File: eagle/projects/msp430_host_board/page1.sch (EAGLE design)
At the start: 5 parts, among them U1 Value

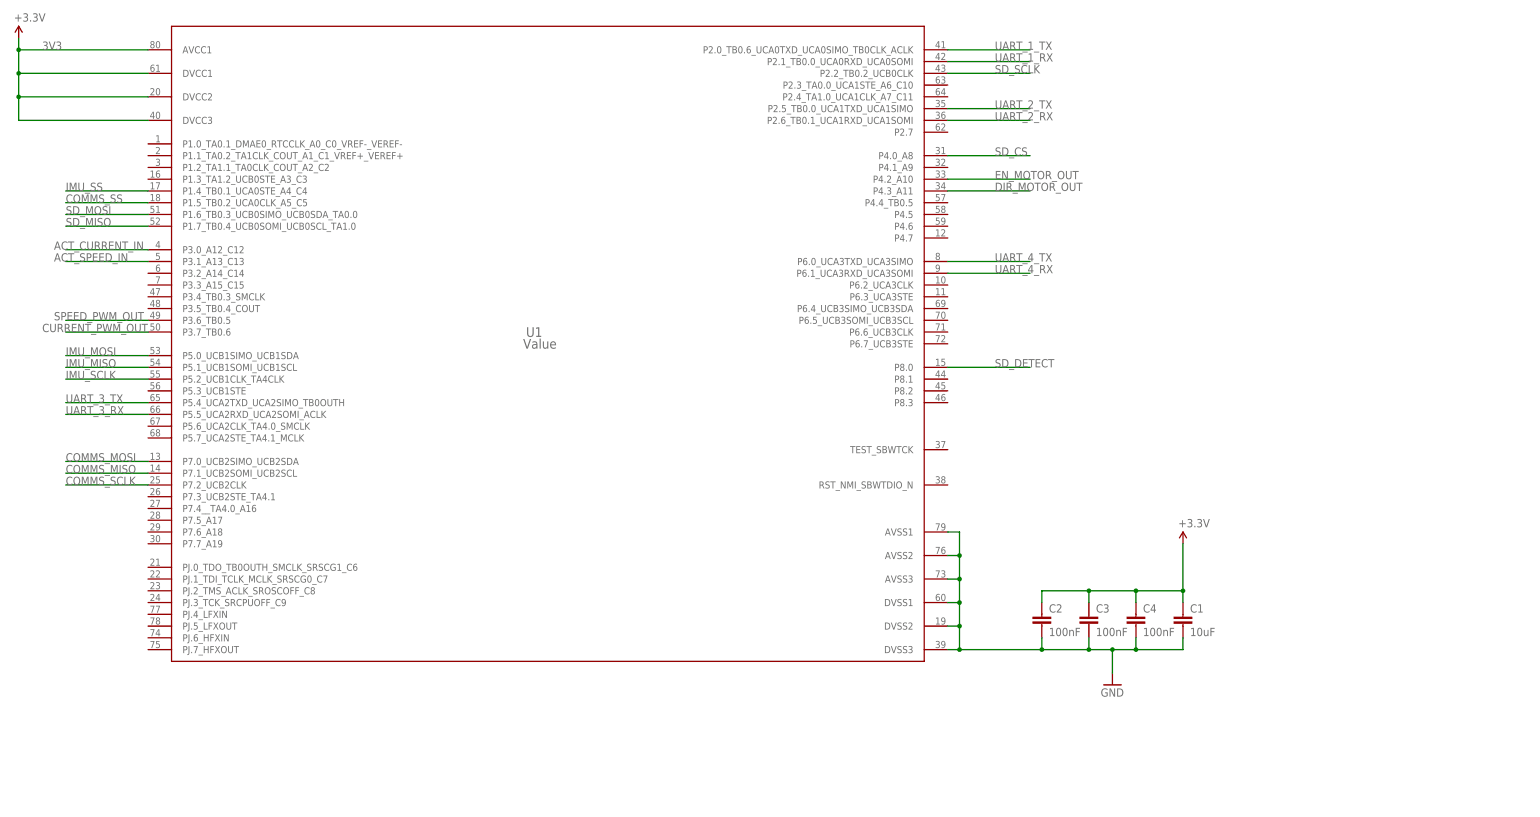
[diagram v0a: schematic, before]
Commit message: Added 22pf cap and LF crystal to schematic
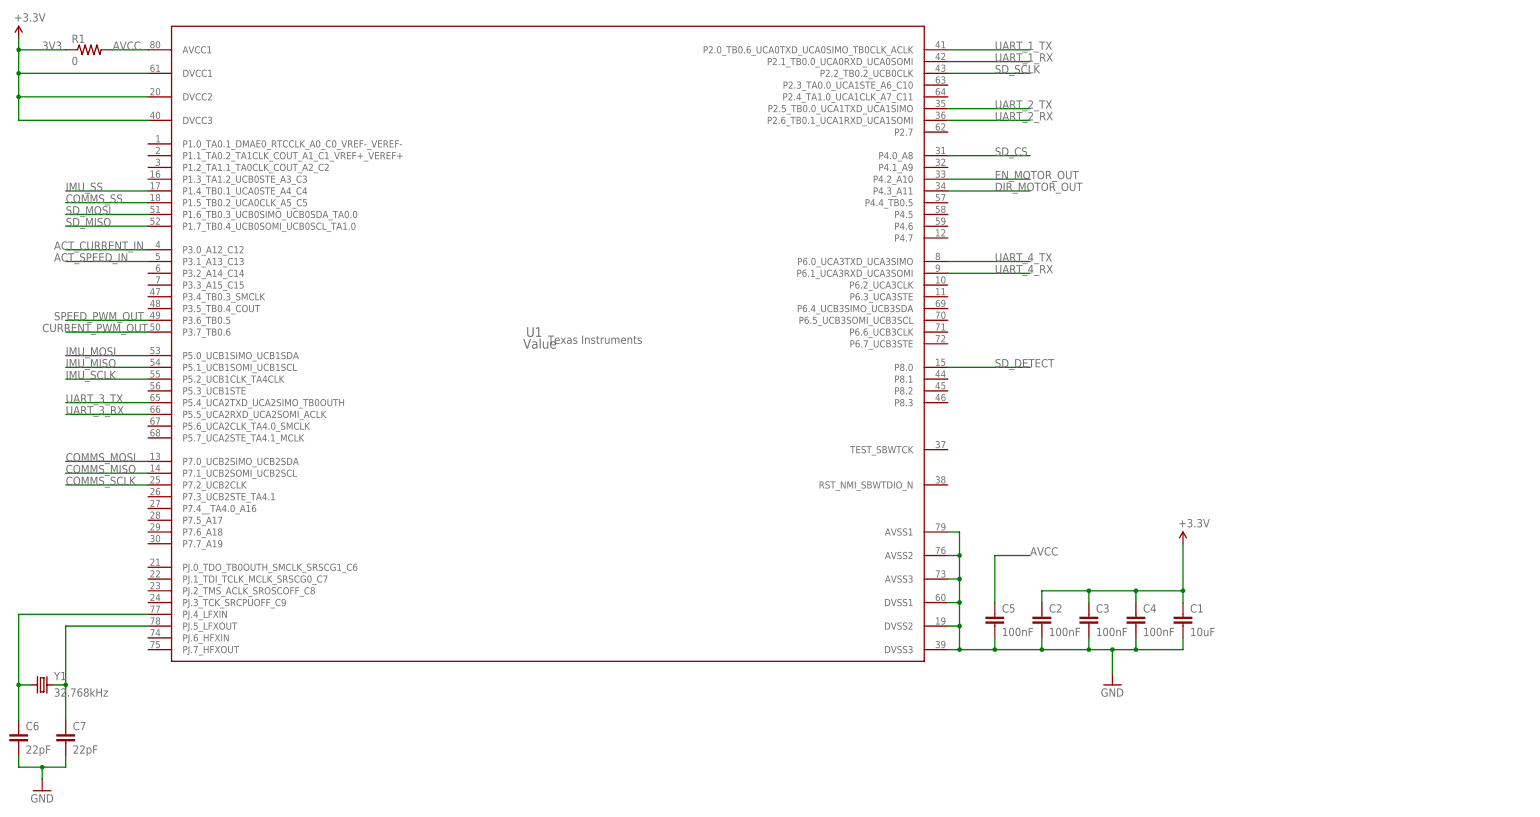
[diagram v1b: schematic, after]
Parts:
- added C5: 100nF, daqcs_host:CAP_100NF0_0603
- added C6, C7: 22pF, daqcs_host:CAP_22PF0_0603
- added R1: 0, daqcs_host:RES_0R0_0603
- added Y1: 32.768kHz, SparkFun-FreqCtrl:CRYSTAL3.2X1.5MM
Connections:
- new net AVCC: C5.1, R1.2, U1.AVCC1
- new net N$1: C6.1, U1.PJ.4_LFXIN, Y1.1
- new net N$2: C7.1, U1.PJ.5_LFXOUT, Y1.2
- net 3V3: now also R1.1; no longer U1.AVCC1
- net GND: now also C5.2, C6.2, C7.2
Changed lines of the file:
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@@
 <setting verticaltext="up"/>
 </settings>
-<grid distance="0.1" unitdist="inch" unit="inch" style="dots" multiple="1" display="yes" altdistance="0.01" altunitdist="inch" altunit="inch"/>
+<grid distance="0.1" unitdist="inch" unit="inch" style="lines" multiple="1" display="no" altdistance="0.01" altunitdist="inch" altunit="inch"/>
 <layers>
 <layer number="1" name="Top" color="4" fill="1" visible="no" active="no"/>
@@
 <part name="C4" library="daqcs_host" deviceset="CAP" device="_0603" technology="_100NF0" value="100nF"/>
 <part name="GND1" library="SparkFun-Aesthetics" deviceset="GND" device=""/>
+<part name="R1" library="daqcs_host" deviceset="RES" device="_0603" technology="_0R0" value="0"/>
+<part name="C5" library="daqcs_host" deviceset="CAP" device="_0603" technology="_100NF0" value="100nF"/>
+<part name="Y1" library="SparkFun-FreqCtrl" deviceset="CRYSTAL" device="3.2X1.5MM" value="32.768kHz"/>
+<part name="C6" library="daqcs_host" deviceset="CAP" device="_0603" technology="_22PF0" value="22pF"/>
+<part name="C7" library="daqcs_host" deviceset="CAP" device="_0603" technology="_22PF0" value="22pF"/>
+<part name="GND2" library="SparkFun-Aesthetics" deviceset="GND" device=""/>
 </parts>
 <sheets>
@@
 </plain>
 <instances>
-<instance part="U1" gate="A" x="43.18" y="48.26"/>
+<instance part="U1" gate="A" x="43.18" y="48.26">
+<attribute name="MANUFACTURER" x="43.18" y="48.26" size="1.778" layer="96"/>
+<attribute name="PARTNUMBER" x="43.18" y="48.26" size="1.778" layer="96" display="off"/>
+</instance>
 <instance part="FRAME1" gate="G$1" x="-78.74" y="-55.88"/>
 <instance part="3V3" gate="G$1" x="-71.12" y="114.3"/>
@@
 <instance part="C4" gate="G$1" x="170.18" y="-12.7"/>
 <instance part="GND1" gate="1" x="165.1" y="-25.4"/>
+<instance part="R1" gate="G$1" x="-55.88" y="111.76"/>
+<instance part="C5" gate="G$1" x="139.7" y="-12.7"/>
+<instance part="Y1" gate="G$1" x="-66.04" y="-25.4"/>
+<instance part="C6" gate="G$1" x="-71.12" y="-38.1"/>
+<instance part="C7" gate="G$1" x="-60.96" y="-38.1"/>
+<instance part="GND2" gate="1" x="-66.04" y="-48.26"/>
 </instances>
 <busses>
@@
 <pinref part="3V3" gate="G$1" pin="3.3V"/>
 <wire x1="-71.12" y1="114.3" x2="-71.12" y2="111.76" width="0.1524" layer="91"/>
-<pinref part="U1" gate="A" pin="AVCC1"/>
-<wire x1="-71.12" y1="111.76" x2="-43.18" y2="111.76" width="0.1524" layer="91"/>
+<pinref part="U1" gate="A" pin="DVCC1"/>
 <wire x1="-71.12" y1="111.76" x2="-71.12" y2="106.68" width="0.1524" layer="91"/>
-<junction x="-71.12" y="111.76"/>
-<pinref part="U1" gate="A" pin="DVCC1"/>
 <wire x1="-71.12" y1="106.68" x2="-43.18" y2="106.68" width="0.1524" layer="91"/>
 <wire x1="-71.12" y1="106.68" x2="-71.12" y2="101.6" width="0.1524" layer="91"/>
@@
 <wire x1="-71.12" y1="96.52" x2="-43.18" y2="96.52" width="0.1524" layer="91"/>
 <label x="-66.04" y="111.76" size="1.778" layer="95"/>
+<pinref part="R1" gate="G$1" pin="1"/>
+<wire x1="-60.96" y1="111.76" x2="-71.12" y2="111.76" width="0.1524" layer="91"/>
+<junction x="-71.12" y="111.76"/>
 </segment>
 <segment>
@@
 <pinref part="U1" gate="A" pin="DVSS3"/>
 <wire x1="129.54" y1="-17.78" x2="132.08" y2="-17.78" width="0.1524" layer="91"/>
-<wire x1="132.08" y1="-17.78" x2="149.86" y2="-17.78" width="0.1524" layer="91"/>
+<wire x1="132.08" y1="-17.78" x2="139.7" y2="-17.78" width="0.1524" layer="91"/>
+<wire x1="139.7" y1="-17.78" x2="149.86" y2="-17.78" width="0.1524" layer="91"/>
 <wire x1="149.86" y1="-17.78" x2="160.02" y2="-17.78" width="0.1524" layer="91"/>
 <wire x1="160.02" y1="-17.78" x2="165.1" y2="-17.78" width="0.1524" layer="91"/>
@@
 <wire x1="165.1" y1="-22.86" x2="165.1" y2="-17.78" width="0.1524" layer="91"/>
 <junction x="165.1" y="-17.78"/>
-</segment>
-</net>
+<pinref part="C5" gate="G$1" pin="2"/>
+<wire x1="139.7" y1="-15.24" x2="139.7" y2="-17.78" width="0.1524" layer="91"/>
+<junction x="139.7" y="-17.78"/>
+</segment>
+<segment>
+<pinref part="C6" gate="G$1" pin="2"/>
+<wire x1="-71.12" y1="-40.64" x2="-71.12" y2="-43.18" width="0.1524" layer="91"/>
+<wire x1="-71.12" y1="-43.18" x2="-66.04" y2="-43.18" width="0.1524" layer="91"/>
+<pinref part="C7" gate="G$1" pin="2"/>
+<wire x1="-66.04" y1="-43.18" x2="-60.96" y2="-43.18" width="0.1524" layer="91"/>
+<wire x1="-60.96" y1="-43.18" x2="-60.96" y2="-40.64" width="0.1524" layer="91"/>
+<pinref part="GND2" gate="1" pin="GND"/>
+<wire x1="-66.04" y1="-45.72" x2="-66.04" y2="-43.18" width="0.1524" layer="91"/>
+<junction x="-66.04" y="-43.18"/>
+</segment>
+</net>
+<net name="AVCC" class="0">
+<segment>
+<pinref part="R1" gate="G$1" pin="2"/>
+<pinref part="U1" gate="A" pin="AVCC1"/>
+<wire x1="-50.8" y1="111.76" x2="-43.18" y2="111.76" width="0.1524" layer="91"/>
+<label x="-50.8" y="111.76" size="1.778" layer="95"/>
+</segment>
+<segment>
+<pinref part="C5" gate="G$1" pin="1"/>
+<wire x1="139.7" y1="-7.62" x2="139.7" y2="2.54" width="0.1524" layer="91"/>
+<wire x1="139.7" y1="2.54" x2="147.32" y2="2.54" width="0.1524" layer="91"/>
+<label x="147.32" y="2.54" size="1.778" layer="95"/>
+</segment>
+</net>
+<net name="N$1" class="0">
+<segment>
+<pinref part="C6" gate="G$1" pin="1"/>
+<wire x1="-71.12" y1="-33.02" x2="-71.12" y2="-25.4" width="0.1524" layer="91"/>
+<pinref part="Y1" gate="G$1" pin="1"/>
+<wire x1="-71.12" y1="-25.4" x2="-68.58" y2="-25.4" width="0.1524" layer="91"/>
+<wire x1="-71.12" y1="-25.4" x2="-71.12" y2="-10.16" width="0.1524" layer="91"/>
+<junction x="-71.12" y="-25.4"/>
+<pinref part="U1" gate="A" pin="PJ.4_LFXIN"/>
+<wire x1="-71.12" y1="-10.16" x2="-43.18" y2="-10.16" width="0.1524" layer="91"/>
+</segment>
+</net>
+<net name="N$2" class="0">
+<segment>
+<pinref part="Y1" gate="G$1" pin="2"/>
+<wire x1="-63.5" y1="-25.4" x2="-60.96" y2="-25.4" width="0.1524" layer="91"/>
+<pinref part="C7" gate="G$1" pin="1"/>
+<wire x1="-60.96" y1="-25.4" x2="-60.96" y2="-33.02" width="0.1524" layer="91"/>
+<wire x1="-60.96" y1="-25.4" x2="-60.96" y2="-12.7" width="0.1524" layer="91"/>
+<junction x="-60.96" y="-25.4"/>
+<pinref part="U1" gate="A" pin="PJ.5_LFXOUT"/>
+<wire x1="-60.96" y1="-12.7" x2="-43.18" y2="-12.7" width="0.1524" layer="91"/>
+</segment>
+</net>

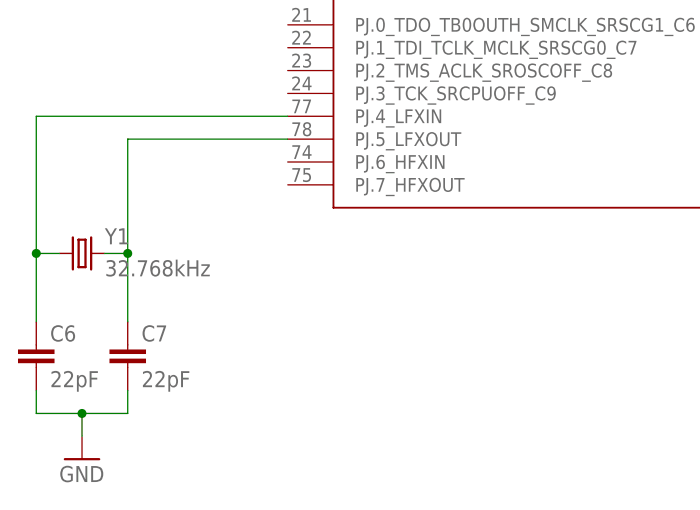
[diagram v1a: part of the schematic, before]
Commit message: Added HF crystal to schematic
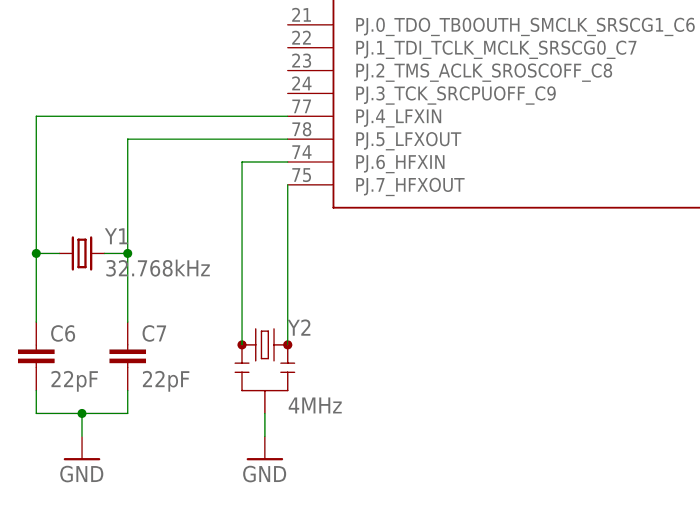
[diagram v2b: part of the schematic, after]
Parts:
- added Y2: 4MHz, SparkFun-FreqCtrl:RESONATOR4MHZ
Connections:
- new net N$3: U1.PJ.6_HFXIN, Y2.1
- new net N$4: U1.PJ.7_HFXOUT, Y2.3
- net GND: now also Y2.2
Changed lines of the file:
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@@
 <part name="C7" library="daqcs_host" deviceset="CAP" device="_0603" technology="_22PF0" value="22pF"/>
 <part name="GND2" library="SparkFun-Aesthetics" deviceset="GND" device=""/>
+<part name="Y2" library="SparkFun-FreqCtrl" deviceset="RESONATOR" device="4MHZ" value="4MHz"/>
+<part name="GND3" library="SparkFun-Aesthetics" deviceset="GND" device=""/>
 </parts>
 <sheets>
@@
 <instance part="C7" gate="G$1" x="-60.96" y="-38.1"/>
 <instance part="GND2" gate="1" x="-66.04" y="-48.26"/>
+<instance part="Y2" gate="G$1" x="-45.72" y="-35.56"/>
+<instance part="GND3" gate="1" x="-45.72" y="-48.26"/>
 </instances>
 <busses>
@@
 <junction x="-66.04" y="-43.18"/>
 </segment>
+<segment>
+<pinref part="Y2" gate="G$1" pin="2"/>
+<pinref part="GND3" gate="1" pin="GND"/>
+<wire x1="-45.72" y1="-43.18" x2="-45.72" y2="-45.72" width="0.1524" layer="91"/>
+</segment>
 </net>
 <net name="AVCC" class="0">
@@
 </segment>
 </net>
+<net name="N$3" class="0">
+<segment>
+<pinref part="U1" gate="A" pin="PJ.6_HFXIN"/>
+<wire x1="-43.18" y1="-15.24" x2="-48.26" y2="-15.24" width="0.1524" layer="91"/>
+<pinref part="Y2" gate="G$1" pin="1"/>
+<wire x1="-48.26" y1="-15.24" x2="-48.26" y2="-35.56" width="0.1524" layer="91"/>
+</segment>
+</net>
+<net name="N$4" class="0">
+<segment>
+<pinref part="U1" gate="A" pin="PJ.7_HFXOUT"/>
+<pinref part="Y2" gate="G$1" pin="3"/>
+<wire x1="-43.18" y1="-17.78" x2="-43.18" y2="-35.56" width="0.1524" layer="91"/>
+</segment>
+</net>
